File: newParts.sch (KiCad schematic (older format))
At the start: 7 parts, among them SW3 SW_SPDT, U2 74HC08, U3 74HC4511D, U4 HEF4518BT, U5 74HC32

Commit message: tiny fixes in annotation
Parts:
- renumbered R10 to R100, SW3 to SW300, U2 to U200, U3 to U300, U4 to U400, U5 to U500
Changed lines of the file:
@@
 $EndComp
 $Comp
-L PB170:74HC08 U2
+L PB170:74HC08 U200
 U 1 1 5FEA6010
 P 1000 1450
-F 0 "U2" H 1025 1717 50  0000 C CNN
+F 0 "U200" H 1025 1717 50  0000 C CNN
 F 1 "74HC08" H 1025 1626 50  0000 C CNN
 F 2 "Housings_SOIC:SOIC-14_3.9x8.7mm_Pitch1.27mm" H 1000 1450 50  0001 C CNN
@@
 $EndComp
 $Comp
-L PB170:74HC08 U2
+L PB170:74HC08 U200
 U 2 1 5FEA6FF4
 P 1800 1450
-F 0 "U2" H 1825 1717 50  0000 C CNN
+F 0 "U200" H 1825 1717 50  0000 C CNN
 F 1 "74HC08" H 1825 1626 50  0000 C CNN
 F 2 "Housings_SOIC:SOIC-14_3.9x8.7mm_Pitch1.27mm" H 1800 1450 50  0001 C CNN
@@
 $EndComp
 $Comp
-L PB170:74HC08 U2
+L PB170:74HC08 U200
 U 3 1 5FEA79A4
 P 2550 1450
-F 0 "U2" H 2575 1717 50  0000 C CNN
+F 0 "U200" H 2575 1717 50  0000 C CNN
 F 1 "74HC08" H 2575 1626 50  0000 C CNN
 F 2 "Housings_SOIC:SOIC-14_3.9x8.7mm_Pitch1.27mm" H 2550 1450 50  0001 C CNN
@@
 $EndComp
 $Comp
-L PB170:74HC08 U2
+L PB170:74HC08 U200
 U 4 1 5FEA7D64
 P 3300 1450
-F 0 "U2" H 3325 1717 50  0000 C CNN
+F 0 "U200" H 3325 1717 50  0000 C CNN
 F 1 "74HC08" H 3325 1626 50  0000 C CNN
 F 2 "Housings_SOIC:SOIC-14_3.9x8.7mm_Pitch1.27mm" H 3300 1450 50  0001 C CNN
@@
 $EndComp
 $Comp
-L PB170:74HC08 U2
+L PB170:74HC08 U200
 U 5 1 5FE8D2BE
 P 4050 1450
-F 0 "U2" H 4280 1496 50  0000 L CNN
+F 0 "U200" H 4280 1496 50  0000 L CNN
 F 1 "74HC08" H 4280 1405 50  0000 L CNN
 F 2 "Housings_SOIC:SOIC-14_3.9x8.7mm_Pitch1.27mm" H 4050 1450 50  0001 C CNN
@@
 $EndComp
 $Comp
-L PB170:74HC4511D U3
+L PB170:74HC4511D U300
 U 1 1 5FE8FF7F
 P 5650 1550
-F 0 "U3" H 5650 2181 50  0000 C CNN
+F 0 "U300" H 5650 2181 50  0000 C CNN
 F 1 "74HC4511D" H 5650 2090 50  0000 C CNN
 F 2 "Housings_SOIC:SOIC-16_3.9x9.9mm_Pitch1.27mm" H 5650 1550 50  0001 C CNN
@@
 $EndComp
 $Comp
-L PB170:HEF4518BT U4
+L PB170:HEF4518BT U400
 U 1 1 5FE95EE3
 P 7150 1550
-F 0 "U4" H 7150 1925 50  0000 C CNN
+F 0 "U400" H 7150 1925 50  0000 C CNN
 F 1 "HEF4518BT" H 7150 1834 50  0000 C CNN
 F 2 "Housings_SOIC:SOIC-16_3.9x9.9mm_Pitch1.27mm" H 7150 1550 50  0001 C CNN
@@
 $EndComp
 $Comp
-L PB170:HEF4518BT U4
+L PB170:HEF4518BT U400
 U 2 1 5FE96A3D
 P 8200 1550
-F 0 "U4" H 8200 1925 50  0000 C CNN
+F 0 "U400" H 8200 1925 50  0000 C CNN
 F 1 "HEF4518BT" H 8200 1834 50  0000 C CNN
 F 2 "Housings_SOIC:SOIC-16_3.9x9.9mm_Pitch1.27mm" H 8200 1550 50  0001 C CNN
@@
 $EndComp
 $Comp
-L PB170:HEF4518BT U4
+L PB170:HEF4518BT U400
 U 3 1 5FE96F23
 P 9350 1550
-F 0 "U4" H 9628 1596 50  0000 L CNN
+F 0 "U400" H 9628 1596 50  0000 L CNN
 F 1 "HEF4518BT" H 9628 1505 50  0000 L CNN
 F 2 "Housings_SOIC:SOIC-16_3.9x9.9mm_Pitch1.27mm" H 9350 1550 50  0001 C CNN
@@
 $EndComp
 $Comp
-L PB170:74HC32 U5
+L PB170:74HC32 U500
 U 1 1 6002CB84
 P 1000 2800
-F 0 "U5" H 975 3075 50  0000 C CNN
+F 0 "U500" H 975 3075 50  0000 C CNN
 F 1 "74HC32" H 975 2984 50  0000 C CNN
 F 2 "Housings_SOIC:SOIC-14_3.9x8.7mm_Pitch1.27mm" H 450 3000 50  0001 C CNN
@@
 $EndComp
 $Comp
-L PB170:74HC32 U5
+L PB170:74HC32 U500
 U 2 1 6002F342
 P 1750 2800
-F 0 "U5" H 1725 3075 50  0000 C CNN
+F 0 "U500" H 1725 3075 50  0000 C CNN
 F 1 "74HC32" H 1725 2984 50  0000 C CNN
 F 2 "Housings_SOIC:SOIC-14_3.9x8.7mm_Pitch1.27mm" H 1200 3000 50  0001 C CNN
@@
 $EndComp
 $Comp
-L PB170:74HC32 U5
+L PB170:74HC32 U500
 U 3 1 6003083A
 P 2500 2800
-F 0 "U5" H 2475 3075 50  0000 C CNN
+F 0 "U500" H 2475 3075 50  0000 C CNN
 F 1 "74HC32" H 2475 2984 50  0000 C CNN
 F 2 "Housings_SOIC:SOIC-14_3.9x8.7mm_Pitch1.27mm" H 1950 3000 50  0001 C CNN
@@
 $EndComp
 $Comp
-L PB170:74HC32 U5
+L PB170:74HC32 U500
 U 4 1 60030FE6
 P 3250 2800
-F 0 "U5" H 3225 3075 50  0000 C CNN
+F 0 "U500" H 3225 3075 50  0000 C CNN
 F 1 "74HC32" H 3225 2984 50  0000 C CNN
 F 2 "Housings_SOIC:SOIC-14_3.9x8.7mm_Pitch1.27mm" H 2700 3000 50  0001 C CNN
@@
 $EndComp
 $Comp
-L PB170:74HC32 U5
+L PB170:74HC32 U500
 U 5 1 60031D42
 P 4100 2800
-F 0 "U5" H 3978 2846 50  0000 L CNN
+F 0 "U500" H 3978 2846 50  0000 L CNN
 F 1 "74HC32" H 3978 2755 50  0000 L CNN
 F 2 "Housings_SOIC:SOIC-14_3.9x8.7mm_Pitch1.27mm" H 3550 3000 50  0001 C CNN
@@
 $EndComp
 $Comp
-L Switch:SW_SPDT SW3
+L Switch:SW_SPDT SW300
 U 1 1 601DAABB
 P 5650 3200
-F 0 "SW3" H 5650 3485 50  0000 C CNN
+F 0 "SW300" H 5650 3485 50  0000 C CNN
 F 1 "SW_SPDT" H 5650 3394 50  0000 C CNN
 F 2 "PB170:toggleSwitch" H 5650 3200 50  0001 C CNN
@@
 P 7050 3450
 AR Path="/601EAE8F" Ref="R?"  Part="1"
-AR Path="/5FEB4D4D/601EAE8F" Ref="R10"  Part="1"
-F 0 "R10" H 7120 3496 50  0000 L CNN
+AR Path="/5FEB4D4D/601EAE8F" Ref="R100"  Part="1"
+F 0 "R100" H 7120 3496 50  0000 L CNN
 F 1 "10k" H 7120 3405 50  0000 L CNN
 F 2 "Resistor_SMD:R_0603_1608Metric" V 6980 3450 50  0001 C CNN

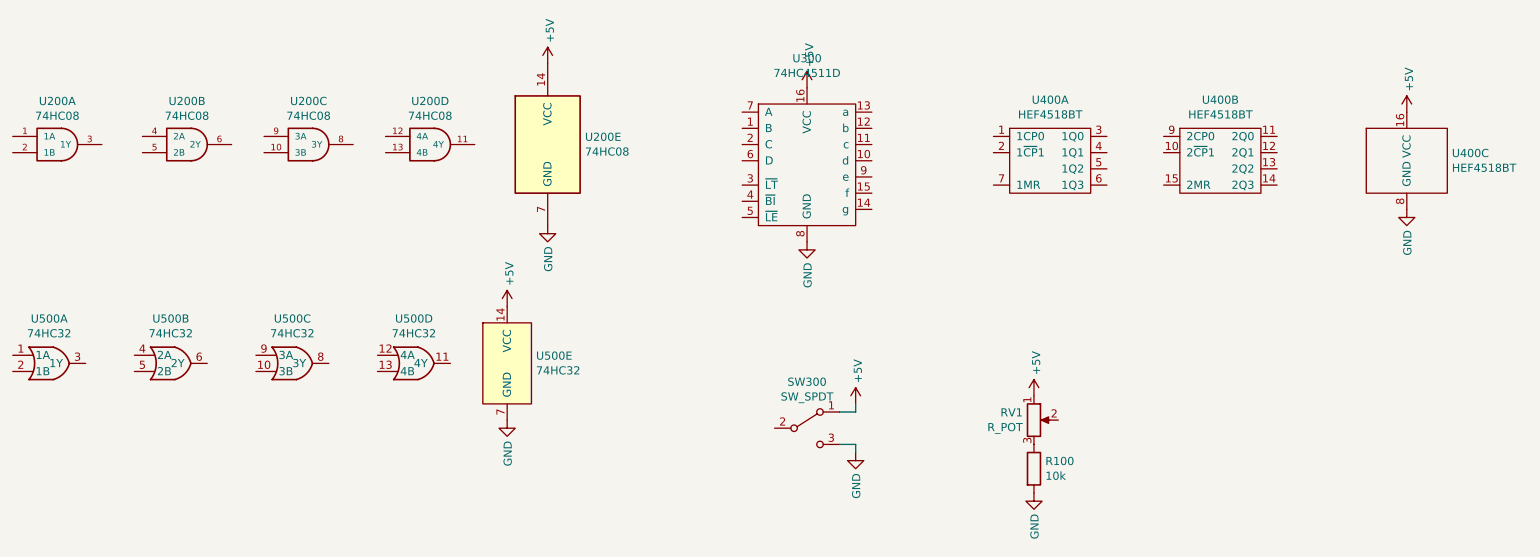
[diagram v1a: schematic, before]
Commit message: Put components on board, set up 3d models of button and switch
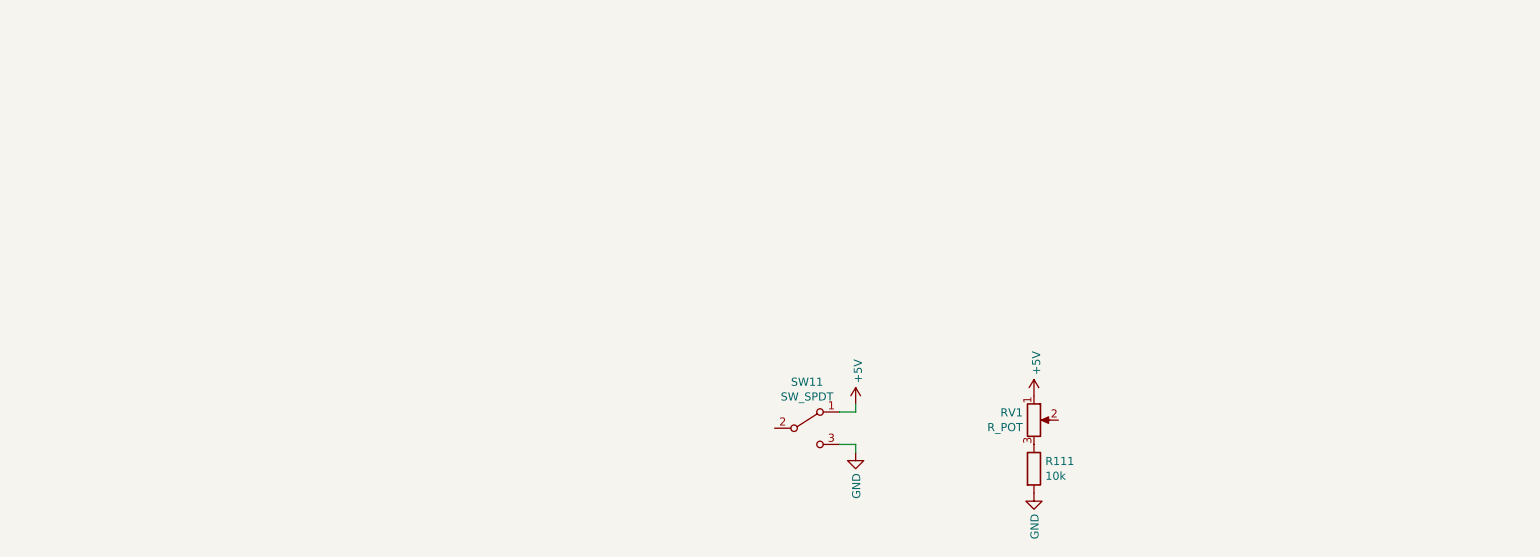
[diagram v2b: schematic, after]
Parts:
- removed U200: 74HC08, Housings_SOIC:SOIC-14_3.9x8.7mm_Pitch1.27mm, symbol PB170:74HC08
- removed U300: 74HC4511D, Housings_SOIC:SOIC-16_3.9x9.9mm_Pitch1.27mm, symbol PB170:74HC4511D
- removed U400: HEF4518BT, Housings_SOIC:SOIC-16_3.9x9.9mm_Pitch1.27mm, symbol PB170:HEF4518BT
- removed U500: 74HC32, Housings_SOIC:SOIC-14_3.9x8.7mm_Pitch1.27mm, symbol PB170:74HC32
- renumbered SW300 to SW11
